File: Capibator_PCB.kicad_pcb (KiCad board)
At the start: 2 copper layers, 101.5 x 64.4 mm, 109 parts, among them J1 FTDI, J10 mist, J12 Water_Level, J14 Battery, J15 Display, J16 Rotary encoder, J17 Temp, J18 Temp2, J19 Water_Pump, J2 LED, J3 C8465, J4 C8465, J5 PJ-002AH, J5 Screw_Terminal_01x02, J6 C8465, J7 Screw_Terminal_01x02, J8 Fan_Exhaust, J9 Fan_Continous, K1 G5NB-1A-E DC12, Q10 AO3406, Q2 AO3406, Q3 AO3406, Q4 AO3406, Q5 AO3406, Q6 AO3406, Q7 SI2301, Q8 AO3406, Q9 AO3406, SW1 SW_Omron_B3FS, SW2 SW_Omron_B3FS, U1 TPS63070RNMR, U2 ESP32-WROOM-32, U3 AMS1117-5.0, U5 PCF8574, U6 MAX17048G_T10, U7 TP4056, U8 DS1307+, U9 G5NB-1A-E DC12, Y1 32.768kHz Quartz Crystal

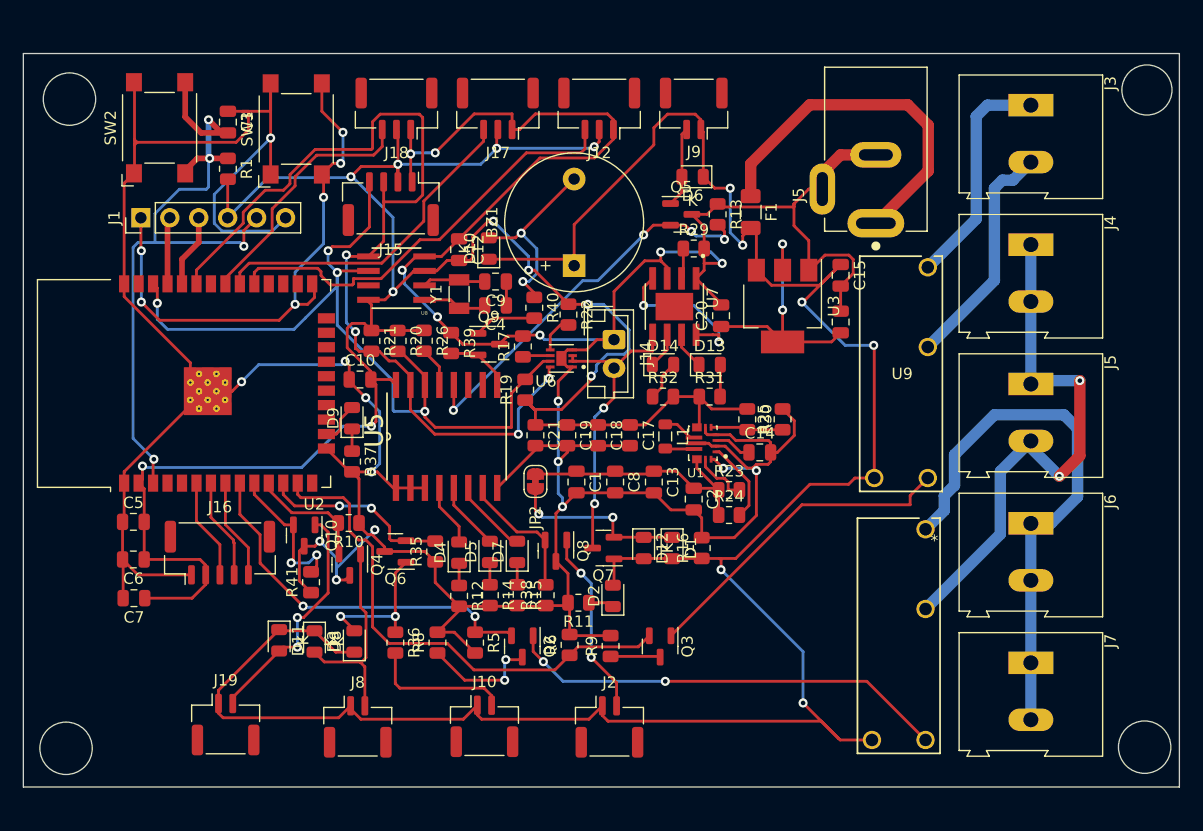
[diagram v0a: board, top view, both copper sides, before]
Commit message: corrected few  mistakes, generated correct bom  with lcsc part numbers
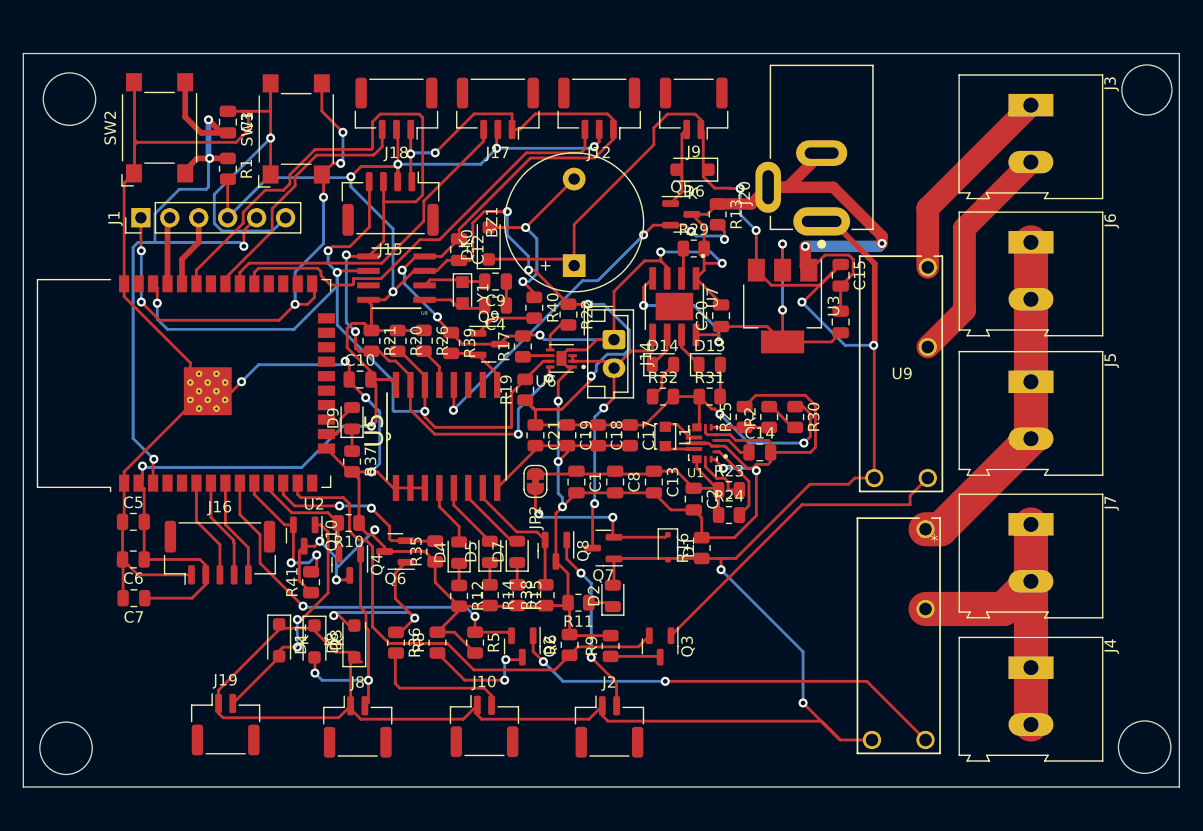
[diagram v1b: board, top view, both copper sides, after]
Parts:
- removed D12: 1N5819, Diode_SMD:D_0805_2012Metric
- removed F1: CAR_FUSE 2A, Fuse:Fuse_1206_3216Metric
- added R2: 3k, Resistor_SMD:R_0805_2012Metric, F.Cu at (192.5, 102.6)
- C12: value C_Small -> 10u
- D1: footprint Diode_SMD:D_0805_2012Metric -> Diode_SMD:D_SOD-323F
- D10, D11, D3, D6, D8: footprint Diode_SMD:D_0805_2012Metric -> Diode_SMD:D_SOD-123F
- J5, J7: value Screw_Terminal_01x02 -> C8465
- L1: footprint Inductor_SMD:L_0805_2012Metric -> Inductor_SMD:L_Murata_LQH2MCNxxxx02_2.0x1.6mm
- R11, R12, R14, R15, R37: value 1K -> 100
- R30: value 213k -> 210k
- R31, R32: value 1.5k -> 100
- Y1: footprint Crystal:Crystal_SMD_3215-2Pin_3.2x1.5mm -> Crystal:Crystal_SMD_2012-2Pin_2.0x1.2mm_HandSoldering
- moved J4 37.1 mm to (215.5, 124.6)
- moved J6 24.7 mm to (215.5, 87.3)
- moved J7 12.2 mm to (215.5, 112.0)
- moved J20 4.76 mm to (197.1, 85.4)
- moved R30 4.21 mm to (194.8, 102.6)
- moved R25 3.34 mm to (190.4, 102.6)
- moved D6 0.62 mm to (185.8, 80.9)
- moved D10 0.44 mm to (167.9, 87.4)
- moved D1 0.38 mm to (183.6, 114.0)
- moved Y1 0.32 mm to (165.6, 91.7), turned to -90 degrees
- moved J5 0.19 mm to (215.5, 99.5)
- moved R36 0.06 mm to (159.8, 122.4)
- renumbered J5 to J20
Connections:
- J20 pad 1: Net-(F1-Pad1) -> +12V
- J5 pad 1: Net-(J4-Pin_1) -> Net-(J5-Pin_1)
- J5 pad 2: Net-(J4-Pin_1) -> Net-(J5-Pin_1)
- J6 pad 1: Net-(J6-Pin_1) -> Net-(J5-Pin_1)
- J6 pad 2: Net-(J6-Pin_1) -> Net-(J5-Pin_1)
- J7 pad 1: Net-(J6-Pin_1) -> Net-(J4-Pin_1)
- J7 pad 2: Net-(J6-Pin_1) -> Net-(J4-Pin_1)
- K1 pad 3: Net-(J6-Pin_1) -> Net-(J5-Pin_1)
- R30 pad 2: /MCU/TPS_FB -> Net-(R2-Pad2)
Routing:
- net Net-(J6-Pin_1): track 48.7 -> 0.00 mm
- net Net-(F1-Pad1): track 31.8 -> 0.00 mm
- net Net-(J5-Pin_1): track 0.00 -> 29.8 mm
- net Net-(J4-Pin_1): track 48.5 -> 27.8 mm, vias 2 -> 0
- net GND: track 425.2 -> 444.7 mm, vias 20 -> 22
- net +12V: track 207.2 -> 222.7 mm
- net +3.3V: track 195.6 -> 208.8 mm, vias 11 -> 13
- net Net-(D8-A): track 13.1 -> 18.0 mm
- net Net-(R2-Pad2): track 0.00 -> 3.04 mm
- net Net-(J3-Pin_1): track 20.2 -> 18.0 mm
- net Net-(D3-A): track 18.4 -> 20.1 mm, vias 0 -> 2
- net /MCU/TPS_FB: track 6.36 -> 5.42 mm
- net Net-(J3-Pin_2): track 20.5 -> 20.0 mm

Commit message: cleaned up tracks, added teardrops, copper fill and improved spacing
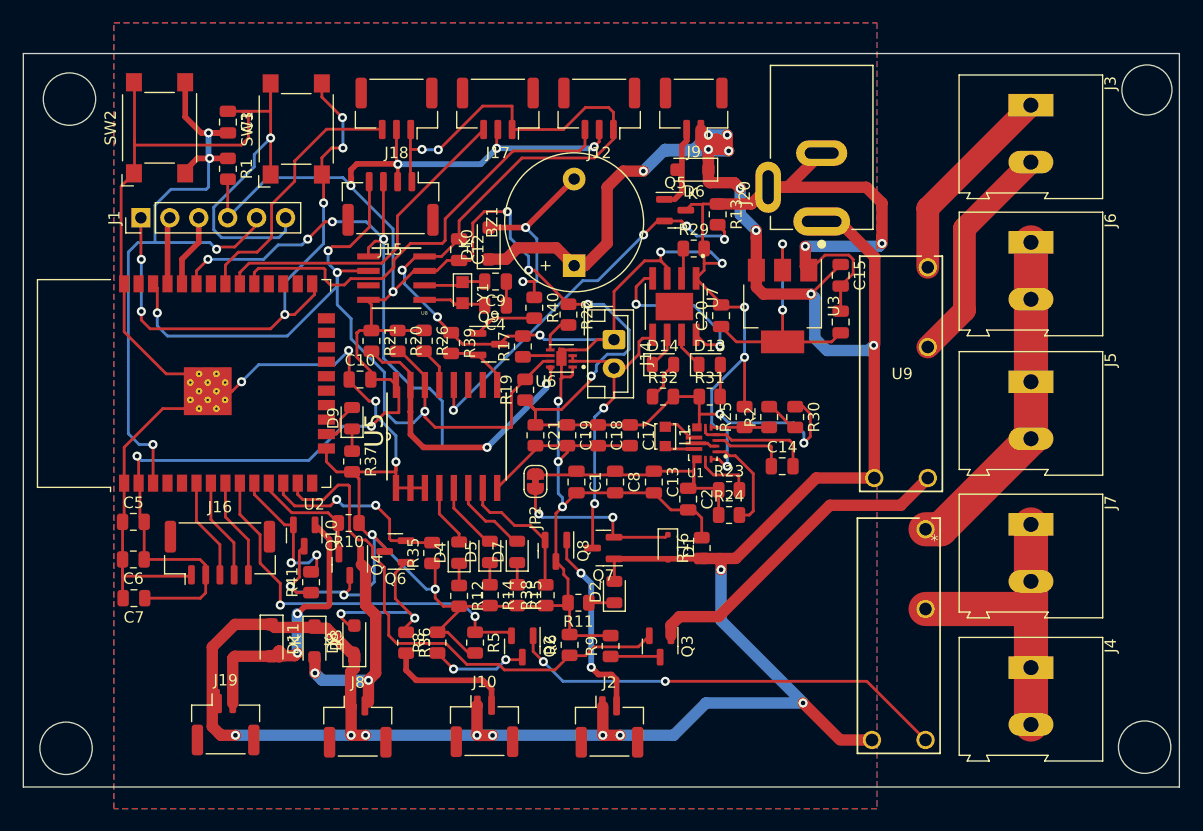
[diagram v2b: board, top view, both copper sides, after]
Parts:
- moved C14 2.31 mm to (193.7, 106.9)
- moved R36 0.89 mm to (160.7, 122.4)
- moved D11 0.67 mm to (148.8, 122.2)
- moved Q5 0.65 mm to (184.3, 84.5)
- moved C2 0.49 mm to (185.4, 109.8)
- moved D2 0.36 mm to (178.9, 118.0)
- moved R35 0.30 mm to (162.9, 114.6)
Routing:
- net +12V: track 222.7 -> 244.1 mm, vias 6 -> 18
- net GND: track 444.7 -> 453.4 mm, vias 22 -> 24
- net /MCU/SDA: track 83.6 -> 78.7 mm, vias 4 -> 6
- net Net-(D11-A): track 20.9 -> 24.9 mm
- net /MCU/TPS_VAUX: track 3.33 -> 6.81 mm
- net /MCU/GPIO0: track 47.8 -> 50.2 mm
- net Net-(Q2-S): track 10.3 -> 8.47 mm
- net +5V: track 36.1 -> 37.8 mm
- net /MCU/turner: track 45.0 -> 46.6 mm
- net Net-(D8-A): track 18.0 -> 16.5 mm
- net /MCU/RESET: track 62.9 -> 61.4 mm
- net Net-(J4-Pin_1): track 27.8 -> 29.3 mm
- net /MCU/PS: track 7.27 -> 8.71 mm
- net /MCU/WATER_LEVEL_DATA: track 37.9 -> 39.3 mm
- net Net-(J10-Pin_2): track 12.4 -> 11.1 mm
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- added copper zone on B.Cu, net GND
- added copper zone on F.Cu, net GND
